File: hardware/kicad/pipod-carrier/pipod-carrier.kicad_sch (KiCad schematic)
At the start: 21 parts, among them J1 Raspberry_Pi_Zero_2W, J2 AudioJack3, SW1 Volume Up, SW2 Volume Down, U1 Adafruit_Seesaw_Encoder, U2 Adafruit 2.2 PiTFT HAT - 320x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, U3 PCM5102A, U4 TPA6132

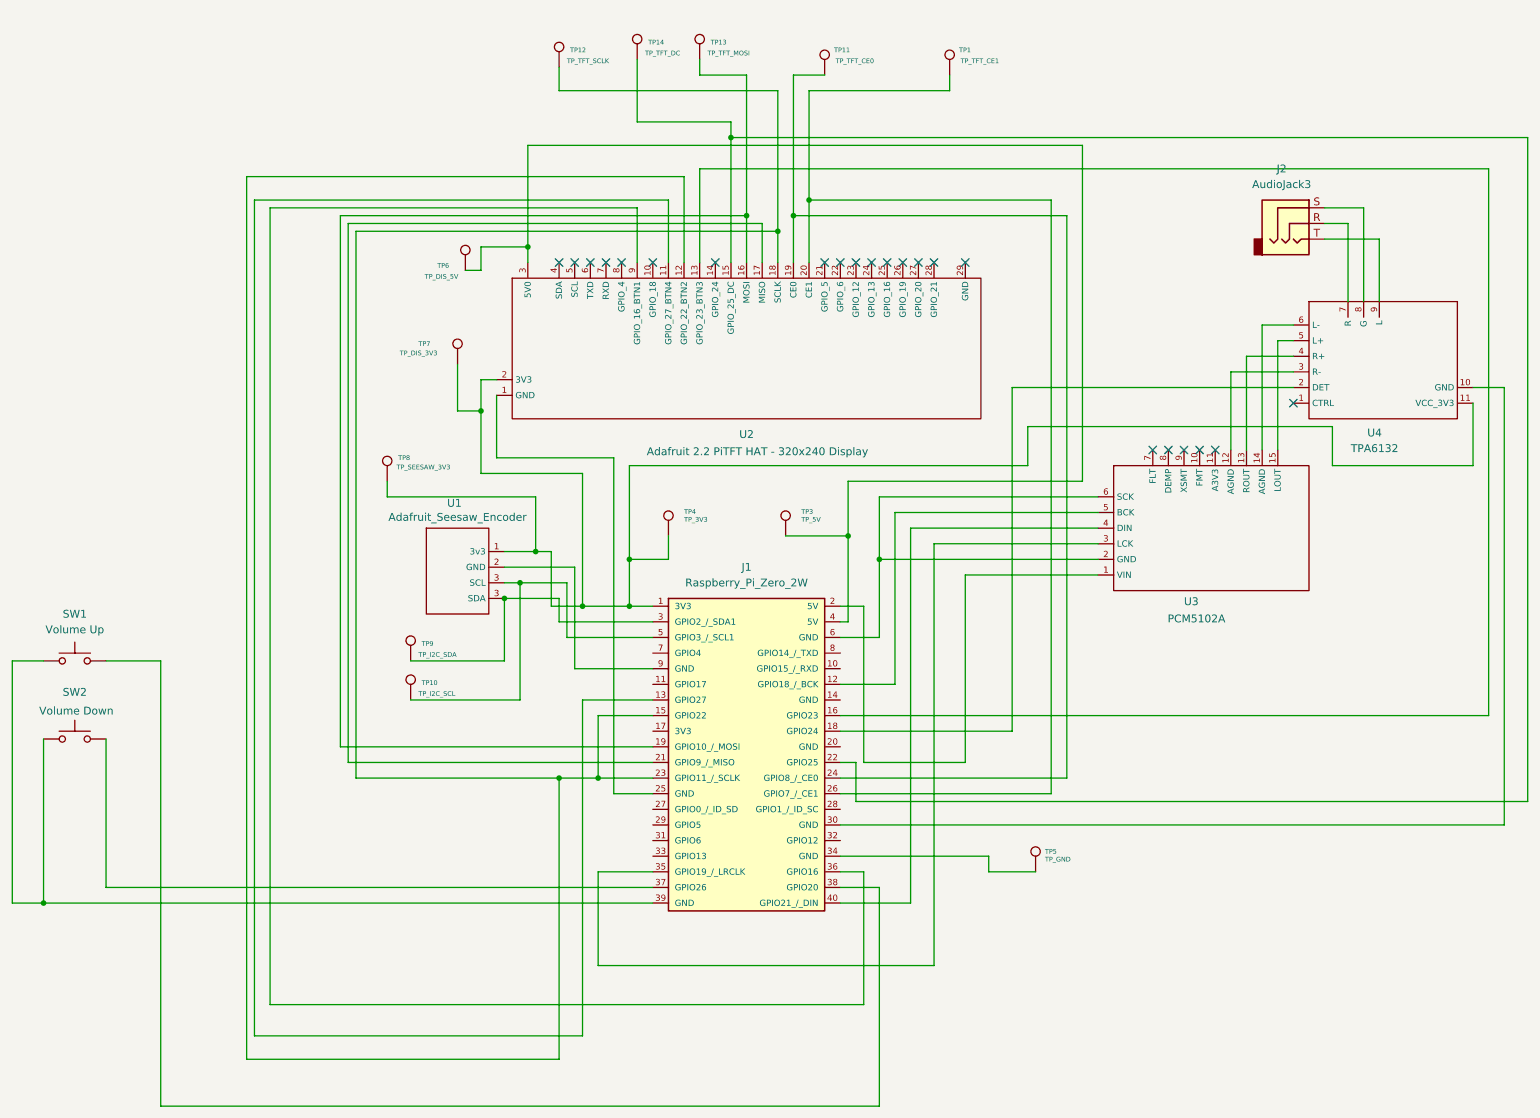
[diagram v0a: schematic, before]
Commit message: cleared schematic errors/warnings
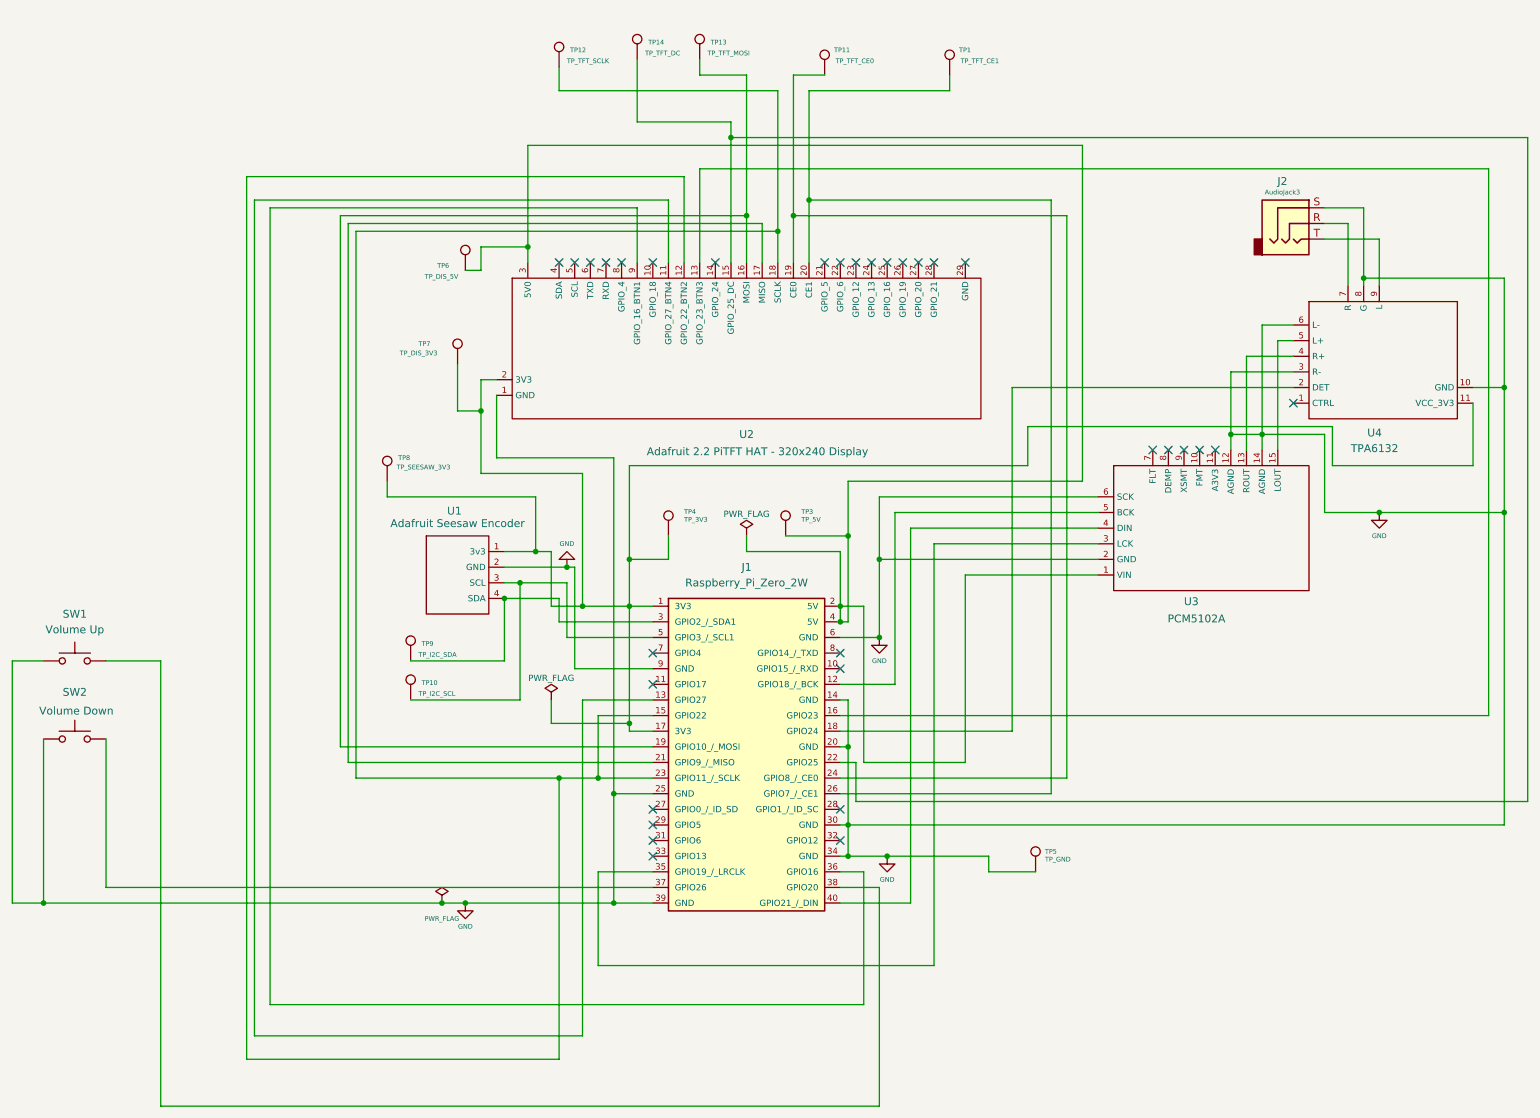
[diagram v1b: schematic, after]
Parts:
- U1: value Adafruit_Seesaw_Encoder -> Adafruit Seesaw Encoder
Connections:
- net GND: now reaches J2.S, U4.8 (G)
- net GND: now also J1.14 (GND), J1.20 (GND), J1.25 (GND), J1.30 (GND), J1.34 (GND), J1.39 (GND), J1.6 (GND), J1.9 (GND), SW1.1, SW2.1, TP5.1, U1.2 (GND), U2.1 (GND), U3.12 (AGND), U3.14 (AGND), U3.2 (GND), U3.6 (SCK), U4.10 (GND), U4.3 (R-), U4.6 (L-)
- net at J1.1 (3V3), TP4.1, TP7.1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: now also J1.17 (3V3)
- net at J1.4 (5V), TP3.1, TP6.1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: now also J1.2 (5V), U3.1 (VIN)
- net at J1.3 (GPIO2_/_SDA1), TP9.1: now also U1.4 (SDA); no longer U1.3 (SDA)
- no-connect marks 22 -> 32
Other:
- moved on the sheet: U1, U4

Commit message: starting footprint assignments for the PCB
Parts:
- SW1, SW2: footprint (none) -> pipod_footprints:SW_Tactile_6x6_RightAngle
- TP1, TP10, TP11, TP12, TP13, TP14, TP3, TP4, TP5, TP6, TP7, TP8, TP9: footprint (none) -> TestPoint:TestPoint_Plated_Hole_D2.0mm
- U1: footprint (none) -> Button_Switch_THT:SW_PUSH_6mm
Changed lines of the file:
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@@
 			)
 		)
-		(property "Footprint" ""
+		(property "Footprint" "TestPoint:TestPoint_Plated_Hole_D2.0mm"
 			(at 111.76 24.13 0)
 			(hide yes)
@@
 			)
 		)
-		(property "Footprint" ""
+		(property "Footprint" "TestPoint:TestPoint_Plated_Hole_D2.0mm"
 			(at 87.63 127 0)
 			(hide yes)
@@
 			)
 		)
-		(property "Footprint" ""
+		(property "Footprint" "TestPoint:TestPoint_Plated_Hole_D2.0mm"
 			(at 129.54 100.33 0)
 			(hide yes)
@@
 			)
 		)
-		(property "Footprint" ""
+		(property "Footprint" "TestPoint:TestPoint_Plated_Hole_D2.0mm"
 			(at 95.25 72.39 0)
 			(hide yes)
@@
 			)
 		)
-		(property "Footprint" ""
+		(property "Footprint" "TestPoint:TestPoint_Plated_Hole_D2.0mm"
 			(at 87.63 120.65 0)
 			(hide yes)
@@
 			)
 		)
-		(property "Footprint" ""
+		(property "Footprint" "TestPoint:TestPoint_Plated_Hole_D2.0mm"
 			(at 154.94 25.4 0)
 			(hide yes)
@@
 			)
 		)
-		(property "Footprint" ""
+		(property "Footprint" "pipod_footprints:SW_Tactile_6x6_RightAngle"
 			(at 27.94 115.57 0)
 			(hide yes)
@@
 			)
 		)
-		(property "Footprint" ""
+		(property "Footprint" "Button_Switch_THT:SW_PUSH_6mm"
 			(at 85.09 129.54 0)
 			(hide yes)
@@
 			)
 		)
-		(property "Footprint" ""
+		(property "Footprint" "TestPoint:TestPoint_Plated_Hole_D2.0mm"
 			(at 148.59 100.33 0)
 			(hide yes)
@@
 			)
 		)
-		(property "Footprint" ""
+		(property "Footprint" "TestPoint:TestPoint_Plated_Hole_D2.0mm"
 			(at 175.26 25.4 0)
 			(hide yes)
@@
 			)
 		)
-		(property "Footprint" ""
+		(property "Footprint" "pipod_footprints:SW_Tactile_6x6_RightAngle"
 			(at 27.94 128.27 0)
 			(hide yes)
@@
 			)
 		)
-		(property "Footprint" ""
+		(property "Footprint" "TestPoint:TestPoint_Plated_Hole_D2.0mm"
 			(at 189.23 154.94 0)
 			(hide yes)
@@
 			)
 		)
-		(property "Footprint" ""
+		(property "Footprint" "TestPoint:TestPoint_Plated_Hole_D2.0mm"
 			(at 83.82 91.44 0)
 			(hide yes)
@@
 			)
 		)
-		(property "Footprint" ""
+		(property "Footprint" "TestPoint:TestPoint_Plated_Hole_D2.0mm"
 			(at 134.62 22.86 0)
 			(hide yes)
@@
 			)
 		)
-		(property "Footprint" ""
+		(property "Footprint" "TestPoint:TestPoint_Plated_Hole_D2.0mm"
 			(at 96.52 57.15 0)
 			(hide yes)
@@
 			)
 		)
-		(property "Footprint" ""
+		(property "Footprint" "TestPoint:TestPoint_Plated_Hole_D2.0mm"
 			(at 124.46 22.86 0)
 			(hide yes)

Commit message: Added PCM5102 and TPA6132 footprints and assigned to schematic
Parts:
- J1: footprint (none) -> Connector_PinSocket_2.54mm:PinSocket_2x20_P2.54mm_Vertical
- J2, U3: footprint (none) -> pipod_footprints:GY-PCM5102_PiPod
- U4: footprint (none) -> pipod_footprints:TPA6132_PiPod
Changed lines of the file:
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@@
 			)
 		)
-		(property "Footprint" ""
+		(property "Footprint" "pipod_footprints:GY-PCM5102_PiPod"
 			(at 226.06 49.53 0)
 			(hide yes)
@@
 			)
 		)
-		(property "Footprint" ""
+		(property "Footprint" "pipod_footprints:TPA6132_PiPod"
 			(at 307.34 49.53 0)
 			(hide yes)
@@
 			)
 		)
-		(property "Footprint" ""
+		(property "Footprint" "Connector_PinSocket_2.54mm:PinSocket_2x20_P2.54mm_Vertical"
 			(at 137.16 135.89 0)
 			(hide yes)
@@
 			)
 		)
-		(property "Footprint" ""
+		(property "Footprint" "pipod_footprints:GY-PCM5102_PiPod"
 			(at 182.88 120.65 0)
 			(hide yes)

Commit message: Added SeeSaw header footprint
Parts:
- U1: footprint Button_Switch_THT:SW_PUSH_6mm -> Connector_PinHeader_2.54mm:PinHeader_1x04_P2.54mm_Vertical
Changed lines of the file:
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@@
 			)
 		)
-		(property "Footprint" "Button_Switch_THT:SW_PUSH_6mm"
+		(property "Footprint" "Connector_PinHeader_2.54mm:PinHeader_1x04_P2.54mm_Vertical"
 			(at 85.09 129.54 0)
 			(hide yes)

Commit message: completed footprint assignments
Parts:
- added J3: Conn_02x06_Odd_Even, Connector_PinHeader_2.54mm:PinHeader_2x06_P2.54mm_Vertical, symbol Connector_Generic:Conn_02x06_Odd_Even
- added J5: Conn_01x02, Connector_PinHeader_2.54mm:PinHeader_1x02_P2.54mm_Vertical, symbol Connector_Generic:Conn_01x02
- J2: footprint pipod_footprints:GY-PCM5102_PiPod -> Connector_Audio:Jack_3.5mm_CUI_SJ1-3523N_Horizontal
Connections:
- net GND: now also J5.1 (Pin_1)
- net TFT_BTN4: now reaches J1.15 (GPIO22), J1.23 (GPIO11_/_SCLK), TP12.1, U2.12 (GPIO_22_BTN2), U2.18 (SCLK)
- net TFT_BTN4: now also J3.3 (Pin_3), J3.9 (Pin_9)
- net 3V3: now reaches J1.1 (3V3), J1.17 (3V3), TP4.1, TP7.1, TP8.1, U1.1 (3v3), U2.2 (3V3), U4.11 (VCC_3V3)
- net 3V3: now also J5.2 (Pin_2)
- net TFT_BTN2: now reaches J1.13 (GPIO27), U2.11 (GPIO_27_BTN4)
- net TFT_BTN2: now also J3.4 (Pin_4)
- net TFT_BTN3: now reaches J1.16 (GPIO23), U2.13 (GPIO_23_BTN3)
- net TFT_BTN3: now also J3.5 (Pin_5)
- net TFT_DC: now reaches J1.22 (GPIO25), TP14.1, U2.15 (GPIO_25_DC)
- net TFT_DC: now also J3.6 (Pin_6)
- net TFT_MOSI: now reaches J1.19 (GPIO10_/_MOSI), TP13.1, U2.16 (MOSI)
- net TFT_MOSI: now also J3.7 (Pin_7)
- net TFT_MISO: now reaches J1.21 (GPIO9_/_MISO), U2.17 (MISO)
- net TFT_MISO: now also J3.8 (Pin_8)
- net TFT_CE1: now reaches J1.24 (GPIO8_/_CE0), TP11.1, U2.19 (CE0)
- net TFT_CE1: now also J3.11 (Pin_11)
- net TFT_CE0: now reaches J1.26 (GPIO7_/_CE1), TP1.1, U2.20 (CE1)
- net TFT_CE0: now also J3.10 (Pin_10)
- net 5V: now reaches J1.2 (5V), J1.4 (5V), TP3.1, TP6.1, U2.3 (5V0), U3.1 (VIN)
- net 5V: now also J3.1 (Pin_1)
- net TFT_BTN1: now reaches J1.36 (GPIO16), U2.9 (GPIO_16_BTN1)
- net TFT_BTN1: now also J3.2 (Pin_2)
- no-connect marks 32 -> 33

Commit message: PCB Layout start
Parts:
- removed J2: AudioJack3, Connector_Audio:Jack_3.5mm_CUI_SJ1-3523N_Horizontal, symbol Connector_Audio:AudioJack3
- added TP15: TP_TFT_MISO, TestPoint:TestPoint_Plated_Hole_D2.0mm, symbol Connector:TestPoint
- J1: footprint Connector_PinSocket_2.54mm:PinSocket_2x20_P2.54mm_Vertical -> Module:Raspberry_Pi_Zero_Socketed_THT_FaceDown_MountingHoles
- TP6: value TP_DIS_5V -> TP_TFT_5V
- TP7: value TP_DIS_3V3 -> TP_TFT_3V3
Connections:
- net GND: no longer U4.8 (G)
- net TFT_BTN4: no longer J1.23 (GPIO11_/_SCLK), J3.9 (Pin_9), TP12.1, U2.18 (SCLK)
- net TFT_MISO: now also TP15.1
- new net TFT_SCLK: J1.23 (GPIO11_/_SCLK), J3.9 (Pin_9), TP12.1, U2.18 (SCLK)
- no-connect marks 33 -> 36
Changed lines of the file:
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@@
 	)
 	(junction
-		(at 260.35 76.2)
-		(diameter 0)
-		(color 0 0 0 0)
-	)
-	(junction
 		(at 97.79 110.49)
 		(diameter 0)
@@
 	)
 	(junction
-		(at 93.98 80.01)
+		(at 139.7 49.53)
 		(diameter 0)
 		(color 0 0 0 0)
 	)
 	(junction
-		(at 237.49 58.42)
+		(at 93.98 80.01)
 		(diameter 0)
 		(color 0 0 0 0)
@@
 	)
 	(junction
-		(at 106.68 139.7)
-		(diameter 0)
-		(color 0 0 0 0)
-	)
-	(junction
 		(at 102.87 102.87)
 		(diameter 0)
@@
 	)
 	(junction
-		(at 113.03 139.7)
-		(diameter 0)
-		(color 0 0 0 0)
-	)
-	(junction
 		(at 115.57 142.24)
 		(diameter 0)
@@
 	)
 	(no_connect
+		(at 234.95 59.69)
+	)
+	(no_connect
 		(at 93.98 35.56)
 	)
 	(no_connect
+		(at 240.03 59.69)
+	)
+	(no_connect
 		(at 109.22 55.88)
 	)
@@
 	)
 	(no_connect
+		(at 237.49 59.69)
+	)
+	(no_connect
 		(at 172.72 55.88)
 	)
@@
 	(wire
 		(pts
-			(xy 237.49 58.42) (xy 260.35 58.42)
-		)
-		(stroke
-			(width 0)
-			(type default)
-		)
-	)
-	(wire
-		(pts
 			(xy 163.83 99.06) (xy 163.83 160.02)
 		)
@@
 	(wire
 		(pts
-			(xy 237.49 46.99) (xy 237.49 58.42)
-		)
-		(stroke
-			(width 0)
-			(type default)
-		)
-	)
-	(wire
-		(pts
 			(xy 17.78 120.65) (xy 17.78 160.02)
 		)
@@
 	(wire
 		(pts
-			(xy 113.03 139.7) (xy 121.92 139.7)
+			(xy 73.66 139.7) (xy 121.92 139.7)
 		)
 		(stroke
@@
 	(wire
 		(pts
-			(xy 106.68 139.7) (xy 113.03 139.7)
-		)
-		(stroke
-			(width 0)
-			(type default)
-		)
-	)
-	(wire
-		(pts
 			(xy 106.68 110.49) (xy 106.68 114.3)
 		)
@@
 	(wire
 		(pts
-			(xy 260.35 58.42) (xy 260.35 76.2)
-		)
-		(stroke
-			(width 0)
-			(type default)
-		)
-	)
-	(wire
-		(pts
 			(xy 22.86 133.35) (xy 22.86 160.02)
 		)
@@
 	(wire
 		(pts
-			(xy 73.66 139.7) (xy 106.68 139.7)
-		)
-		(stroke
-			(width 0)
-			(type default)
-		)
-	)
-	(wire
-		(pts
 			(xy 134.62 55.88) (xy 135.89 55.88)
 		)
@@
 	(wire
 		(pts
-			(xy 231.14 49.53) (xy 234.95 49.53)
+			(xy 129.54 55.88) (xy 128.27 55.88)
 		)
 		(stroke
@@
 	(wire
 		(pts
-			(xy 129.54 55.88) (xy 128.27 55.88)
+			(xy 106.68 129.54) (xy 121.92 129.54)
 		)
 		(stroke
@@
 	(wire
 		(pts
-			(xy 231.14 52.07) (xy 240.03 52.07)
-		)
-		(stroke
-			(width 0)
-			(type default)
-		)
-	)
-	(wire
-		(pts
 			(xy 102.87 102.87) (xy 105.41 102.87)
 		)
@@
 	(wire
 		(pts
-			(xy 237.49 46.99) (xy 231.14 46.99)
-		)
-		(stroke
-			(width 0)
-			(type default)
-		)
-	)
-	(wire
-		(pts
 			(xy 158.75 116.84) (xy 152.4 116.84)
 		)
@@
 	(wire
 		(pts
-			(xy 240.03 52.07) (xy 240.03 59.69)
-		)
-		(stroke
-			(width 0)
-			(type default)
-		)
-	)
-	(wire
-		(pts
 			(xy 153.67 147.32) (xy 260.35 147.32)
 		)
@@
 	(wire
 		(pts
-			(xy 237.49 58.42) (xy 237.49 59.69)
-		)
-		(stroke
-			(width 0)
-			(type default)
-		)
-	)
-	(wire
-		(pts
 			(xy 182.88 82.55) (xy 232.41 82.55)
 		)
@@
 	(wire
 		(pts
-			(xy 106.68 139.7) (xy 106.68 185.42)
-		)
-		(stroke
-			(width 0)
-			(type default)
-		)
-	)
-	(wire
-		(pts
 			(xy 107.95 105.41) (xy 109.22 105.41)
 		)
@@
 	(wire
 		(pts
-			(xy 264.16 35.56) (xy 134.62 35.56)
+			(xy 139.7 22.86) (xy 139.7 49.53)
 		)
 		(stroke
@@
 	(wire
 		(pts
-			(xy 22.86 120.65) (xy 17.78 120.65)
+			(xy 264.16 35.56) (xy 134.62 35.56)
 		)
 		(stroke
@@
 	(wire
 		(pts
-			(xy 147.32 55.88) (xy 147.32 45.72)
+			(xy 22.86 120.65) (xy 17.78 120.65)
 		)
 		(stroke
@@
 	(wire
 		(pts
-			(xy 234.95 49.53) (xy 234.95 59.69)
+			(xy 147.32 55.88) (xy 147.32 45.72)
 		)
 		(stroke
@@
 	(wire
 		(pts
-			(xy 113.03 129.54) (xy 113.03 139.7)
-		)
-		(stroke
-			(width 0)
-			(type default)
-		)
-	)
-	(wire
-		(pts
 			(xy 93.98 74.93) (xy 93.98 80.01)
 		)
@@
 	(wire
 		(pts
-			(xy 121.92 129.54) (xy 113.03 129.54)
+			(xy 194.31 106.68) (xy 172.72 106.68)
 		)
 		(stroke
@@
 	(wire
 		(pts
-			(xy 194.31 106.68) (xy 172.72 106.68)
+			(xy 176.53 154.94) (xy 184.15 154.94)
 		)
 		(stroke
@@
 	(wire
 		(pts
-			(xy 176.53 154.94) (xy 184.15 154.94)
+			(xy 106.68 129.54) (xy 106.68 185.42)
 		)
 		(stroke
@@
 	)
 	(symbol
-		(lib_id "Connector_Audio:AudioJack3")
-		(at 226.06 49.53 0)
-		(unit 1)
-		(body_style 1)
-		(exclude_from_sim no)
-		(in_bom yes)
-		(on_board yes)
-		(in_pos_files yes)
-		(dnp no)
-		(property "Reference" "J2"
-			(at 224.282 42.672 0)
-			(show_name no)
-			(do_not_autoplace no)
-			(effects
-				(font
-					(size 1.27 1.27)
-				)
-			)
-		)
-		(property "Value" "AudioJack3"
-			(at 224.282 44.45 0)
-			(show_name no)
-			(do_not_autoplace no)
-			(effects
-				(font
-					(size 0.762 0.762)
-				)
-			)
-		)
-		(property "Footprint" "Connector_Audio:Jack_3.5mm_CUI_SJ1-3523N_Horizontal"
-			(at 226.06 49.53 0)
-			(hide yes)
-			(show_name no)
-			(do_not_autoplace no)
-			(effects
-				(font
-					(size 1.27 1.27)
-				)
-			)
-		)
-		(property "Datasheet" ""
-			(at 226.06 49.53 0)
-			(hide yes)
-			(show_name no)
-			(do_not_autoplace no)
-			(effects
-				(font
-					(size 1.27 1.27)
-				)
-			)
-		)
-		(property "Description" "Audio Jack, 3 Poles (Stereo / TRS)"
-			(at 226.06 49.53 0)
-			(hide yes)
-			(show_name no)
-			(do_not_autoplace no)
-			(effects
-				(font
-					(size 1.27 1.27)
-				)
-			)
-		)
-		(pin "T"
-		)
-		(pin "R"
-		)
-		(pin "S"
-		)
-		(instances
-			(project "pipod-carrier"
-				(path "/7155fab1-9c9a-41b5-92ad-f730b415b976"
-					(reference "J2")
-					(unit 1)
-				)
-			)
-		)
-	)
-	(symbol
 		(lib_id "Connector:TestPoint")
 		(at 106.68 24.13 0)
@@
 			)
 		)
-		(property "Value" "TP_DIS_3V3"
+		(property "Value" "TP_TFT_3V3"
 			(at 80.772 70.612 0)
 			(show_name no)
@@
 			)
 		)
-		(property "Footprint" "Connector_PinSocket_2.54mm:PinSocket_2x20_P2.54mm_Vertical"
+		(property "Footprint" "Module:Raspberry_Pi_Zero_Socketed_THT_FaceDown_MountingHoles"
 			(at 137.16 135.89 0)
 			(hide yes)
@@
 			)
 		)
-		(property "Value" "TP_DIS_5V"
+		(property "Value" "TP_TFT_5V"
 			(at 84.836 58.166 0)
 			(show_name no)
@@
 					(unit 1)
 				)
+			)
+		)
+	)
+	(symbol
+		(lib_id "Connector:TestPoint")
+		(at 139.7 22.86 0)
+		(unit 1)
+		(body_style 1)
+		(exclude_from_sim no)
+		(in_bom yes)
+		(on_board yes)
+		(in_pos_files yes)
+		(dnp no)
+		(property "Reference" "TP15"
+			(at 141.478 20.066 0)
+			(show_name no)
+			(do_not_autoplace no)
+			(effects
+				(font
+					(size 0.762 0.762)
+				)
+				(justify left)
+			)
+		)
+		(property "Value" "TP_TFT_MISO"
+			(at 140.97 21.844 0)
+			(show_name no)
+			(do_not_autoplace no)
+			(effects
+				(font
+					(size 0.762 0.762)
+				)
+				(justify left)
+			)
+		)
+		(property "Footprint" "TestPoint:TestPoint_Plated_Hole_D2.0mm"
+			(at 144.78 22.86 0)
+			(hide yes)
+			(show_name no)
+			(do_not_autoplace no)
+			(effects
+				(font
+					(size 1.27 1.27)
+				)
+			)
+		)
+		(property "Datasheet" ""
+			(at 144.78 22.86 0)
+			(hide yes)
+			(show_name no)
+			(do_not_autoplace no)
+			(effects
+				(font
+					(size 1.27 1.27)
+				)
+			)
+		)
+		(property "Description" "test point"
+			(at 139.7 22.86 0)
+			(hide yes)
+			(show_name no)
+			(do_not_autoplace no)
+			(effects
+				(font
+					(size 1.27 1.27)
+				)
+			)
+		)
+		(pin "1"
+		)
+		(instances
+			(project "pipod-carrier"
+				(path "/7155fab1-9c9a-41b5-92ad-f730b415b976"
+					(reference "TP15")
+					(unit 1)
+				)
